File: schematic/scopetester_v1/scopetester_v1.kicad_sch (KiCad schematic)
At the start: 43 parts, among them J1 CON_PWR, J2 Conn_01x04, J3 AVR_ISP, SW1 SW_Push, U1 ATmega8A-P, Y1 12MHz

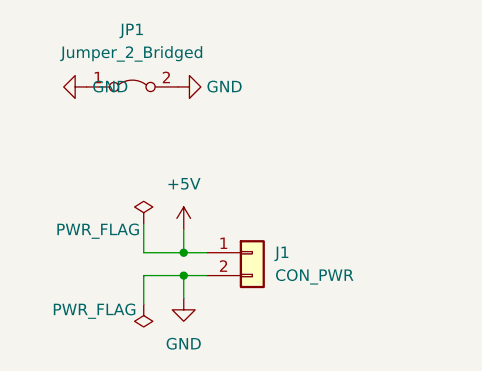
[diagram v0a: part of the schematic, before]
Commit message: Finalized PCB layout (edition 1)
The DRC error of 'mission connection between items' was solved using a
phony track on the front side. This is just to satisfy KiCad because it
does not seem to understand that jumper is actually bridged.
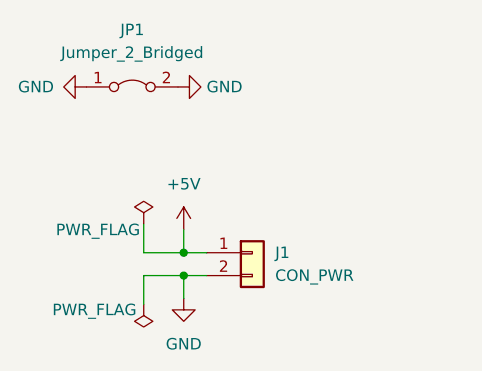
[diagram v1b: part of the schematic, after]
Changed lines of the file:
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@@
   )
   (symbol (lib_id "power:GND") (at 27.305 45.72 270) (unit 1)
-    (in_bom yes) (on_board yes) (fields_autoplaced)
-    (property "Reference" "#PWR?" (id 0) (at 20.955 45.72 0)
-      (effects (font (size 1.27 1.27)) hide)
-    )
-    (property "Value" "GND" (id 1) (at 27.94 45.7199 90)
+    (in_bom yes) (on_board yes)
+    (property "Reference" "#PWR0118" (id 0) (at 20.955 45.72 0)
+      (effects (font (size 1.27 1.27)) hide)
+    )
+    (property "Value" "GND" (id 1) (at 19.685 45.72 90)
       (effects (font (size 1.27 1.27)) (justify left))
     )
@@
   (symbol (lib_id "power:GND") (at 37.465 45.72 90) (unit 1)
     (in_bom yes) (on_board yes) (fields_autoplaced)
-    (property "Reference" "#PWR?" (id 0) (at 43.815 45.72 0)
+    (property "Reference" "#PWR0117" (id 0) (at 43.815 45.72 0)
       (effects (font (size 1.27 1.27)) hide)
     )
@@
       (reference "#PWR0116") (unit 1) (value "+5V") (footprint "")
     )
+    (path "/49d74109-df68-473a-922a-f2d20aa21baf"
+      (reference "#PWR0117") (unit 1) (value "GND") (footprint "")
+    )
     (path "/43b02ddd-f584-4f99-ba88-aa75ee88b79d"
-      (reference "#PWR?") (unit 1) (value "GND") (footprint "")
-    )
-    (path "/49d74109-df68-473a-922a-f2d20aa21baf"
-      (reference "#PWR?") (unit 1) (value "GND") (footprint "")
+      (reference "#PWR0118") (unit 1) (value "GND") (footprint "")
     )
     (path "/d296a615-c4ba-40da-b84d-31d01d3ec12b"

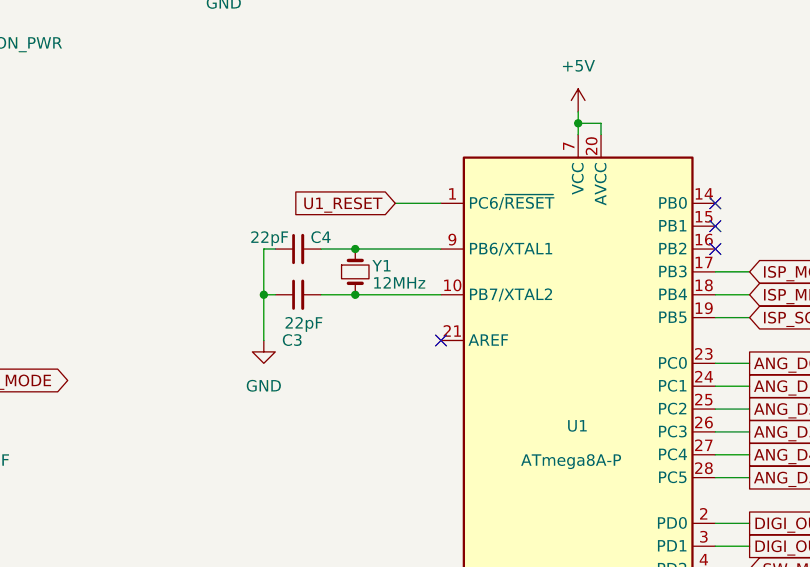
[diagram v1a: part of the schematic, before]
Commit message: Now using 16MHz clock instead of 12MHz
This increases the waveform frequencies by 33.3%.
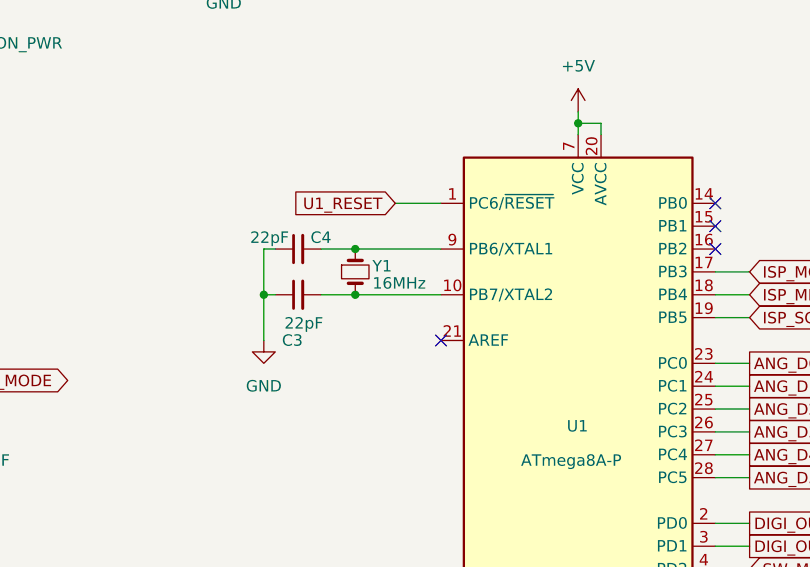
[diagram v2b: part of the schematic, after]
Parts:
- Y1: value 12MHz -> 16MHz
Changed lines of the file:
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@@
       (effects (font (size 1.27 1.27)) (justify left))
     )
-    (property "Value" "12MHz" (id 1) (at 91.44 93.345 90)
+    (property "Value" "16MHz" (id 1) (at 91.44 93.345 90)
       (effects (font (size 1.27 1.27)) (justify left))
     )
@@
     )
     (path "/3ffcb15a-c4e8-4f14-8a7f-117409243806"
-      (reference "Y1") (unit 1) (value "12MHz") (footprint "Crystal:Crystal_HC49-4H_Vertical")
-    )
-  )
+      (reference "Y1") (unit 1) (value "16MHz") (footprint "Crystal:Crystal_HC49-4H_Vertical")
+    )
+  )
